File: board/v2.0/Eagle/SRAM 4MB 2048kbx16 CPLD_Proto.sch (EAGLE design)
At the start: 26 parts, among them IC1 AS6C3216-55, IC2 74LCX245MTC, IC3 74LCX245MTC, IC4 74LCX245MTC, IC5 74LCX541TTR, IC6 74LCX541TTR, IC7 74LCX541TTR, IC8 XC9536_44VQ, IC9 TLV70033DDCT, SW1 RAM/Disk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

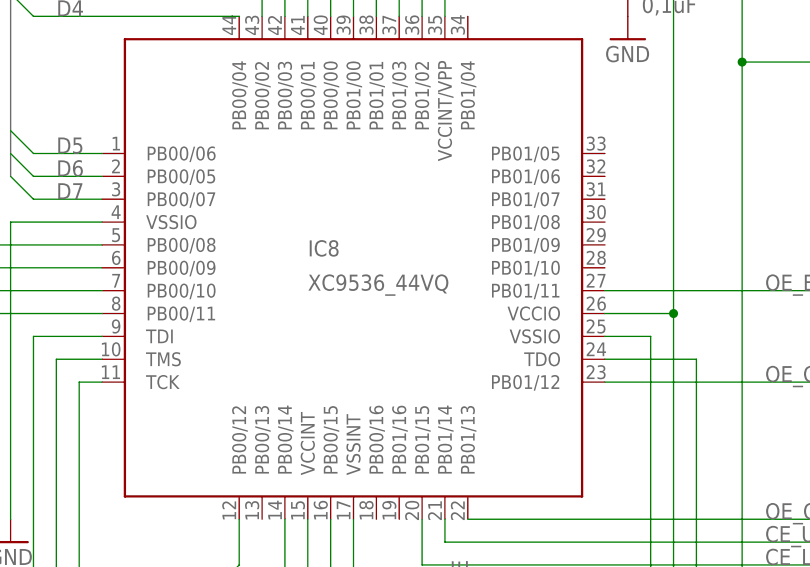
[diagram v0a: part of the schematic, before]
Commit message: Small change in the boards v2.0 and v2.1
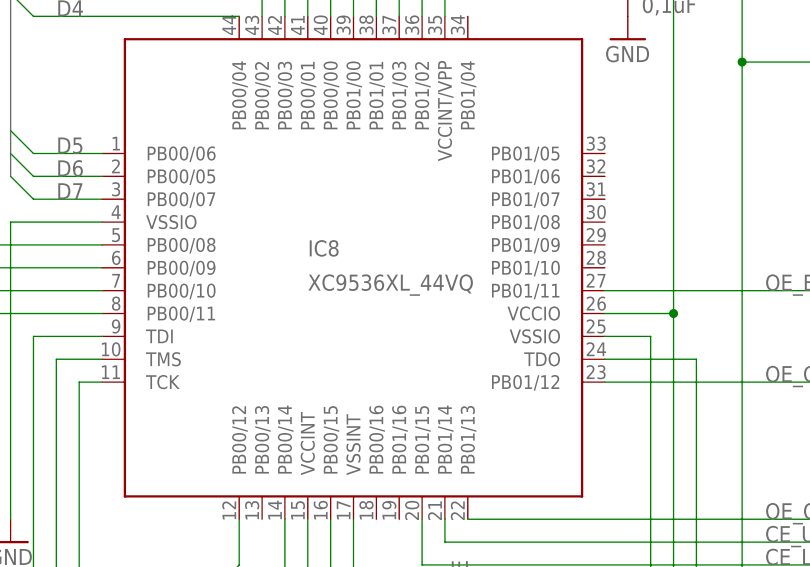
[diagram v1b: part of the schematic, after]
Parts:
- IC8: value XC9536_44VQ -> XC9536XL_44VQ
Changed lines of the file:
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@@
 <part name="GND8" library="supply1" deviceset="GND" device=""/>
 <part name="GND11" library="supply1" deviceset="GND" device=""/>
-<part name="IC8" library="xilinx-xc9" deviceset="XC9536_44VQ" device=""/>
+<part name="IC8" library="xilinx-xc9" deviceset="XC9536_44VQ" device="" value="XC9536XL_44VQ"/>
 <part name="GND2" library="supply1" deviceset="GND" device=""/>
 <part name="GND3" library="supply1" deviceset="GND" device=""/>
